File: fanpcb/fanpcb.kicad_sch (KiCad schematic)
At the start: 0 parts

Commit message: fanpcb str + layout erstellt
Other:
- added sheet FAN (fan.kicad_sch)
- added sheet FAN1 (fan.kicad_sch)
- added sheet FAN2 (fan.kicad_sch)
- added sheet PSU (psu.kicad_sch)
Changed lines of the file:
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@@
 	(generator_version "10.0")
 	(paper "A4")
+	(sheet
+		(at 50.8 63.5)
+		(size 12.7 12.7)
+		(exclude_from_sim no)
+		(in_bom yes)
+		(on_board yes)
+		(dnp no)
+		(fields_autoplaced yes)
+		(stroke
+			(width 0.1524)
+			(type solid)
+		)
+		(fill
+			(color 0 0 0 0)
+		)
+		(property "Sheetname" "FAN"
+			(at 50.8 62.7884 0)
+			(show_name no)
+			(do_not_autoplace no)
+			(effects
+				(font
+					(size 1.27 1.27)
+				)
+				(justify left bottom)
+			)
+		)
+		(property "Sheetfile" "fan.kicad_sch"
+			(at 50.8 76.7846 0)
+			(show_name no)
+			(do_not_autoplace no)
+			(effects
+				(font
+					(size 1.27 1.27)
+				)
+				(justify left top)
+			)
+		)
+		(instances
+			(project "fanpcb"
+				(path "/70212b9f-75b5-4ad8-b5df-8c30fcda9509"
+					(page "2")
+				)
+			)
+		)
+	)
+	(sheet
+		(at 50.8 38.1)
+		(size 12.7 12.7)
+		(exclude_from_sim no)
+		(in_bom yes)
+		(on_board yes)
+		(dnp no)
+		(fields_autoplaced yes)
+		(stroke
+			(width 0.1524)
+			(type solid)
+		)
+		(fill
+			(color 0 0 0 0)
+		)
+		(property "Sheetname" "PSU"
+			(at 50.8 37.3884 0)
+			(show_name no)
+			(do_not_autoplace no)
+			(effects
+				(font
+					(size 1.27 1.27)
+				)
+				(justify left bottom)
+			)
+		)
+		(property "Sheetfile" "psu.kicad_sch"
+			(at 50.8 51.3846 0)
+			(show_name no)
+			(do_not_autoplace no)
+			(effects
+				(font
+					(size 1.27 1.27)
+				)
+				(justify left top)
+			)
+		)
+		(instances
+			(project "fanpcb"
+				(path "/70212b9f-75b5-4ad8-b5df-8c30fcda9509"
+					(page "5")
+				)
+			)
+		)
+	)
+	(sheet
+		(at 50.8 114.3)
+		(size 12.7 12.7)
+		(exclude_from_sim no)
+		(in_bom yes)
+		(on_board yes)
+		(dnp no)
+		(fields_autoplaced yes)
+		(stroke
+			(width 0.1524)
+			(type solid)
+		)
+		(fill
+			(color 0 0 0 0)
+		)
+		(property "Sheetname" "FAN2"
+			(at 50.8 113.5884 0)
+			(show_name no)
+			(do_not_autoplace no)
+			(effects
+				(font
+					(size 1.27 1.27)
+				)
+				(justify left bottom)
+			)
+		)
+		(property "Sheetfile" "fan.kicad_sch"
+			(at 50.8 127.5846 0)
+			(show_name no)
+			(do_not_autoplace no)
+			(effects
+				(font
+					(size 1.27 1.27)
+				)
+				(justify left top)
+			)
+		)
+		(instances
+			(project "fanpcb"
+				(path "/70212b9f-75b5-4ad8-b5df-8c30fcda9509"
+					(page "4")
+				)
+			)
+		)
+	)
+	(sheet
+		(at 50.8 88.9)
+		(size 12.7 12.7)
+		(exclude_from_sim no)
+		(in_bom yes)
+		(on_board yes)
+		(dnp no)
+		(fields_autoplaced yes)
+		(stroke
+			(width 0.1524)
+			(type solid)
+		)
+		(fill
+			(color 0 0 0 0)
+		)
+		(property "Sheetname" "FAN1"
+			(at 50.8 88.1884 0)
+			(show_name no)
+			(do_not_autoplace no)
+			(effects
+				(font
+					(size 1.27 1.27)
+				)
+				(justify left bottom)
+			)
+		)
+		(property "Sheetfile" "fan.kicad_sch"
+			(at 50.8 102.1846 0)
+			(show_name no)
+			(do_not_autoplace no)
+			(effects
+				(font
+					(size 1.27 1.27)
+				)
+				(justify left top)
+			)
+		)
+		(instances
+			(project "fanpcb"
+				(path "/70212b9f-75b5-4ad8-b5df-8c30fcda9509"
+					(page "3")
+				)
+			)
+		)
+	)
 	(sheet_instances
 		(path "/"

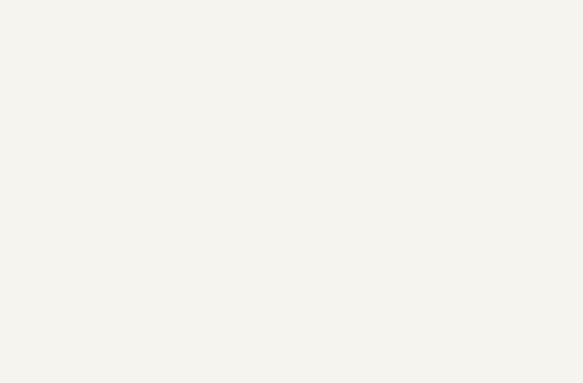
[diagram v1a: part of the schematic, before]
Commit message: Mounting Holes added, gerber updated
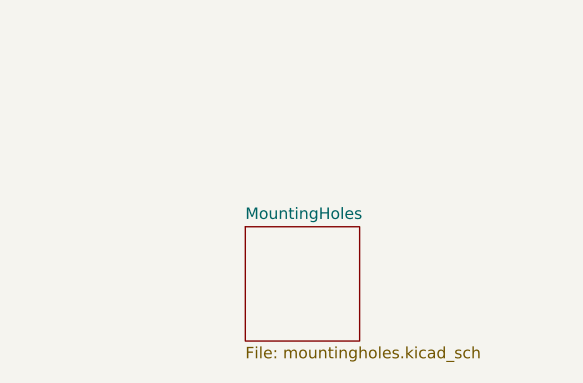
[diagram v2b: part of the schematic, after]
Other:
- added sheet MountingHoles (mountingholes.kicad_sch)
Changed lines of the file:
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@@
+	)
+	(sheet
+		(at 254 139.7)
+		(size 12.7 12.7)
+		(exclude_from_sim no)
+		(in_bom yes)
+		(on_board yes)
+		(dnp no)
+		(fields_autoplaced yes)
+		(stroke
+			(width 0.1524)
+			(type solid)
+		)
+		(fill
+			(color 0 0 0 0)
+		)
+		(property "Sheetname" "MountingHoles"
+			(at 254 138.9884 0)
+			(show_name no)
+			(do_not_autoplace no)
+			(effects
+				(font
+					(size 1.27 1.27)
+				)
+				(justify left bottom)
+			)
+		)
+		(property "Sheetfile" "mountingholes.kicad_sch"
+			(at 254 152.9846 0)
+			(show_name no)
+			(do_not_autoplace no)
+			(effects
+				(font
+					(size 1.27 1.27)
+				)
+				(justify left top)
+			)
+		)
+		(instances
+			(project "fanpcb"
+				(path "/70212b9f-75b5-4ad8-b5df-8c30fcda9509"
+					(page "6")
+				)
+			)
+		)
 	)
 	(sheet
